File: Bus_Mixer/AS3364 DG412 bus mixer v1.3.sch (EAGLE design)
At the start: 121 parts, among them IC1 PCA9539PW, IC10 DG412-J, IC11 DG412-J, IC2 TL074JT, IC3 TL072JT, IC4 TL074JT, IC5 TL072JT, IC6 TL072JT, IC8 DG412-J, IC9 DG412-J

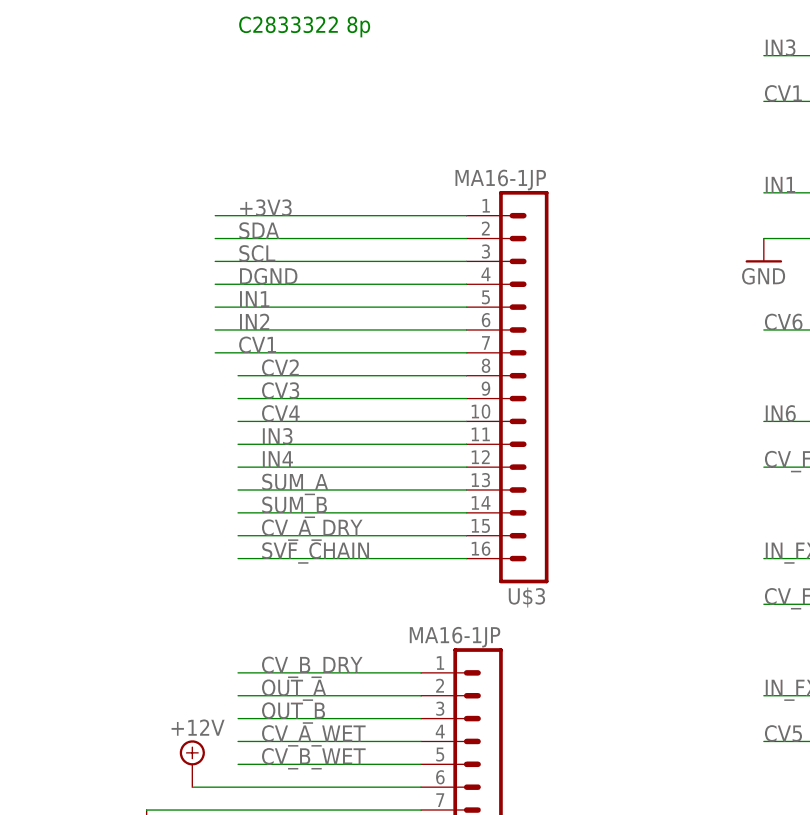
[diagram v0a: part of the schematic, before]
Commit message: Changed connector values
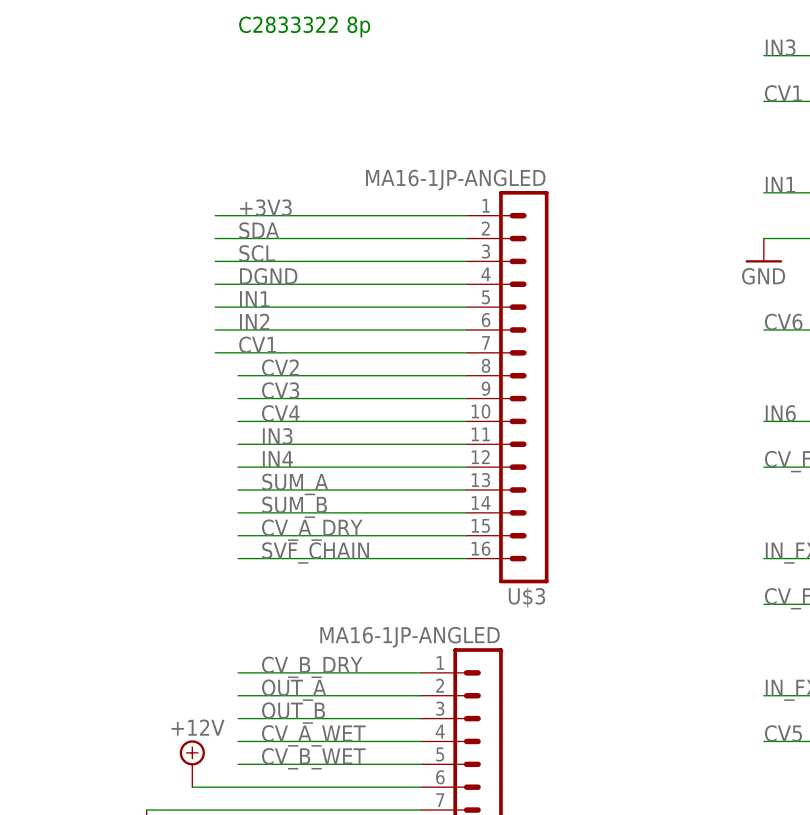
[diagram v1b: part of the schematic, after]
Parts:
- U$2, U$3: value MA16-1JP -> MA16-1JP-ANGLED
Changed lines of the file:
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@@
 <part name="IC5" library="joakim" deviceset="TL072J" device="T" value="TL072JT"/>
 <part name="R69" library="rcl" library_urn="urn:adsk.eagle:library:334" deviceset="R-EU_" device="R0402" package3d_urn="urn:adsk.eagle:package:23547/3" value="47k"/>
-<part name="U$2" library="joakim" deviceset="MA16-1J" device="P"/>
-<part name="U$3" library="joakim" deviceset="MA16-1J" device="P"/>
+<part name="U$2" library="joakim" deviceset="MA16-1J" device="P" value="MA16-1JP-ANGLED"/>
+<part name="U$3" library="joakim" deviceset="MA16-1J" device="P" value="MA16-1JP-ANGLED"/>
 </parts>
 <sheets>

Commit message: Updated
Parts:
- C13, C14, C15, C24, C25, C26, C27: device joakim:C-EU-J -> joakim:C-EU-J0402
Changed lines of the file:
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@@
 <part name="IC3" library="joakim" deviceset="TL072J" device="T" value="TL072JT"/>
 <part name="C18" library="rcl" library_urn="urn:adsk.eagle:library:334" deviceset="C-EU" device="C0402" package3d_urn="urn:adsk.eagle:package:23626/2" value="100nF"/>
-<part name="C13" library="joakim" deviceset="C-EU-J" device="" value="5nF"/>
+<part name="C13" library="joakim" deviceset="C-EU-J" device="0402" value="5nF"/>
 <part name="GND9" library="supply1" library_urn="urn:adsk.eagle:library:371" deviceset="GND" device=""/>
 <part name="DA2" library="joakim" deviceset="AS3364" device="D"/>
@@
 <part name="GND17" library="supply1" library_urn="urn:adsk.eagle:library:371" deviceset="GND" device=""/>
 <part name="GND18" library="supply1" library_urn="urn:adsk.eagle:library:371" deviceset="GND" device=""/>
-<part name="C14" library="joakim" deviceset="C-EU-J" device="" value="5nF"/>
+<part name="C14" library="joakim" deviceset="C-EU-J" device="0402" value="5nF"/>
 <part name="GND19" library="supply1" library_urn="urn:adsk.eagle:library:371" deviceset="GND" device=""/>
 <part name="DA3" library="joakim" deviceset="AS3364" device="D"/>
@@
 <part name="GND37" library="supply1" library_urn="urn:adsk.eagle:library:371" deviceset="GND" device=""/>
 <part name="IC6" library="joakim" deviceset="TL072J" device="T" value="TL072JT"/>
-<part name="C15" library="joakim" deviceset="C-EU-J" device="" value="5nF"/>
+<part name="C15" library="joakim" deviceset="C-EU-J" device="0402" value="5nF"/>
 <part name="GND38" library="supply1" library_urn="urn:adsk.eagle:library:371" deviceset="GND" device=""/>
 <part name="DA1" library="joakim" deviceset="AS3364" device="D"/>
@@
 <part name="GND13" library="supply1" library_urn="urn:adsk.eagle:library:371" deviceset="GND" device=""/>
 <part name="GND14" library="supply1" library_urn="urn:adsk.eagle:library:371" deviceset="GND" device=""/>
-<part name="C24" library="joakim" deviceset="C-EU-J" device="" value="33pF"/>
-<part name="C25" library="joakim" deviceset="C-EU-J" device="" value="33pF"/>
-<part name="C26" library="joakim" deviceset="C-EU-J" device="" value="33pF"/>
-<part name="C27" library="joakim" deviceset="C-EU-J" device="" value="33pF"/>
+<part name="C24" library="joakim" deviceset="C-EU-J" device="0402" value="33pF"/>
+<part name="C25" library="joakim" deviceset="C-EU-J" device="0402" value="33pF"/>
+<part name="C26" library="joakim" deviceset="C-EU-J" device="0402" value="33pF"/>
+<part name="C27" library="joakim" deviceset="C-EU-J" device="0402" value="33pF"/>
 <part name="GND26" library="supply1" library_urn="urn:adsk.eagle:library:371" deviceset="GND" device=""/>
 <part name="R49" library="rcl" library_urn="urn:adsk.eagle:library:334" deviceset="R-EU_" device="R0402" package3d_urn="urn:adsk.eagle:package:23547/3" value="47k"/>

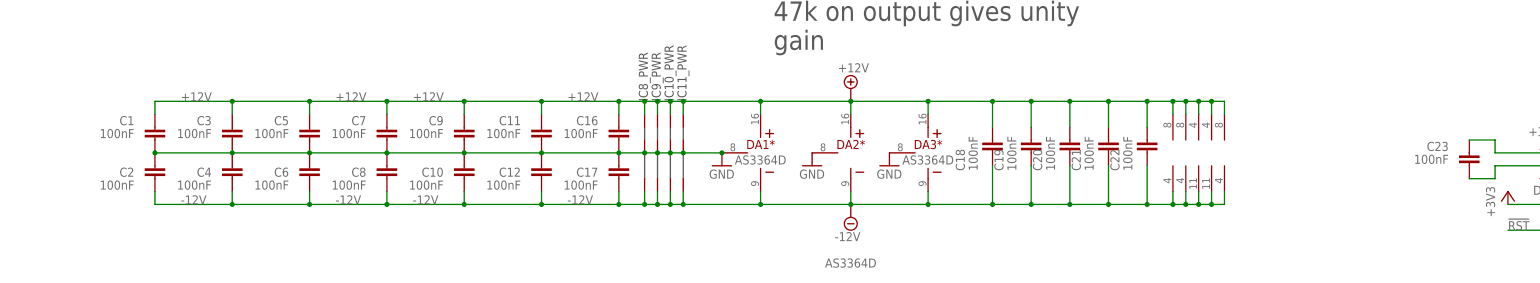
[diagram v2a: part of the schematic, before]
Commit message: Updated decoupling caps. Tested with JLCPCB
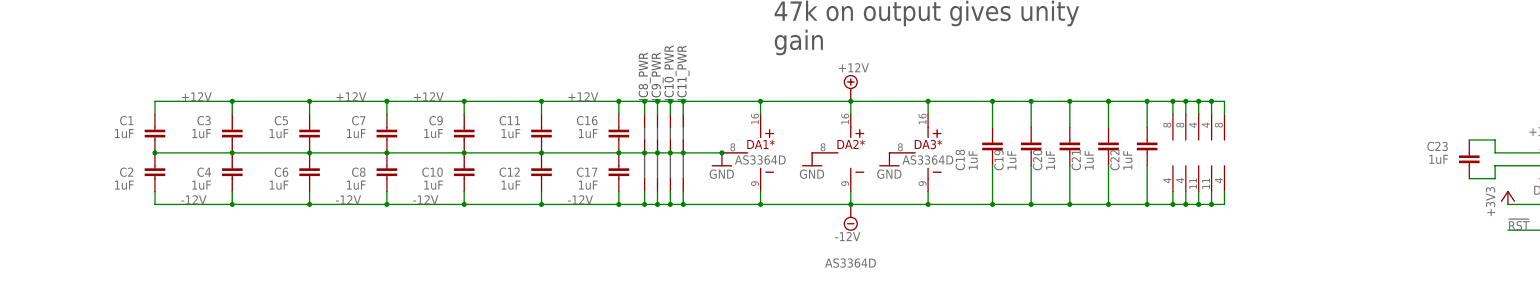
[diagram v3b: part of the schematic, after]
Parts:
- C1, C10, C11, C12, C16, C17, C2, C3, C4, C5, C6, C7, C8, C9: value 100nF -> 1uF; device rcl:C-EUC0402 -> joakim:C-EU-J0402
- C18, C19, C20, C21, C22, C23: value 100nF -> 1uF
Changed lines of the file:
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@@
 <part name="R3" library="rcl" library_urn="urn:adsk.eagle:library:334" deviceset="R-EU_" device="R0402" package3d_urn="urn:adsk.eagle:package:23547/3" value="22k"/>
 <part name="R6" library="rcl" library_urn="urn:adsk.eagle:library:334" deviceset="R-EU_" device="R0402" package3d_urn="urn:adsk.eagle:package:23547/3" value="22k"/>
-<part name="C17" library="rcl" library_urn="urn:adsk.eagle:library:334" deviceset="C-EU" device="C0402" package3d_urn="urn:adsk.eagle:package:23626/2" value="100nF"/>
-<part name="C16" library="rcl" library_urn="urn:adsk.eagle:library:334" deviceset="C-EU" device="C0402" package3d_urn="urn:adsk.eagle:package:23626/2" value="100nF"/>
+<part name="C17" library="joakim" deviceset="C-EU-J" device="0402" value="1uF"/>
+<part name="C16" library="joakim" deviceset="C-EU-J" device="0402" value="1uF"/>
 <part name="R38" library="rcl" library_urn="urn:adsk.eagle:library:334" deviceset="R-EU_" device="R0402" package3d_urn="urn:adsk.eagle:package:23547/3" value="100R"/>
 <part name="GND5" library="supply1" library_urn="urn:adsk.eagle:library:371" deviceset="GND" device=""/>
@@
 <part name="GND7" library="supply1" library_urn="urn:adsk.eagle:library:371" deviceset="GND" device=""/>
 <part name="GND8" library="supply1" library_urn="urn:adsk.eagle:library:371" deviceset="GND" device=""/>
-<part name="C19" library="rcl" library_urn="urn:adsk.eagle:library:334" deviceset="C-EU" device="C0402" package3d_urn="urn:adsk.eagle:package:23626/2" value="100nF"/>
+<part name="C19" library="rcl" library_urn="urn:adsk.eagle:library:334" deviceset="C-EU" device="C0402" package3d_urn="urn:adsk.eagle:package:23626/2" value="1uF"/>
 <part name="GND10" library="supply1" library_urn="urn:adsk.eagle:library:371" deviceset="GND" device=""/>
 <part name="IC3" library="joakim" deviceset="TL072J" device="T" value="TL072JT"/>
-<part name="C18" library="rcl" library_urn="urn:adsk.eagle:library:334" deviceset="C-EU" device="C0402" package3d_urn="urn:adsk.eagle:package:23626/2" value="100nF"/>
+<part name="C18" library="rcl" library_urn="urn:adsk.eagle:library:334" deviceset="C-EU" device="C0402" package3d_urn="urn:adsk.eagle:package:23626/2" value="1uF"/>
 <part name="C13" library="joakim" deviceset="C-EU-J" device="0402" value="5nF"/>
 <part name="GND9" library="supply1" library_urn="urn:adsk.eagle:library:371" deviceset="GND" device=""/>
@@
 <part name="R67" library="rcl" library_urn="urn:adsk.eagle:library:334" deviceset="R-EU_" device="R0402" package3d_urn="urn:adsk.eagle:package:23547/3" value="47k"/>
 <part name="R65" library="rcl" library_urn="urn:adsk.eagle:library:334" deviceset="R-EU_" device="R0402" package3d_urn="urn:adsk.eagle:package:23547/3" value="47k"/>
-<part name="C20" library="rcl" library_urn="urn:adsk.eagle:library:334" deviceset="C-EU" device="C0402" package3d_urn="urn:adsk.eagle:package:23626/2" value="100nF"/>
-<part name="C21" library="rcl" library_urn="urn:adsk.eagle:library:334" deviceset="C-EU" device="C0402" package3d_urn="urn:adsk.eagle:package:23626/2" value="100nF"/>
-<part name="C22" library="rcl" library_urn="urn:adsk.eagle:library:334" deviceset="C-EU" device="C0402" package3d_urn="urn:adsk.eagle:package:23626/2" value="100nF"/>
+<part name="C20" library="rcl" library_urn="urn:adsk.eagle:library:334" deviceset="C-EU" device="C0402" package3d_urn="urn:adsk.eagle:package:23626/2" value="1uF"/>
+<part name="C21" library="rcl" library_urn="urn:adsk.eagle:library:334" deviceset="C-EU" device="C0402" package3d_urn="urn:adsk.eagle:package:23626/2" value="1uF"/>
+<part name="C22" library="rcl" library_urn="urn:adsk.eagle:library:334" deviceset="C-EU" device="C0402" package3d_urn="urn:adsk.eagle:package:23626/2" value="1uF"/>
 <part name="GND20" library="supply1" library_urn="urn:adsk.eagle:library:371" deviceset="GND" device=""/>
-<part name="C11" library="rcl" library_urn="urn:adsk.eagle:library:334" deviceset="C-EU" device="C0402" package3d_urn="urn:adsk.eagle:package:23626/2" value="100nF"/>
-<part name="C12" library="rcl" library_urn="urn:adsk.eagle:library:334" deviceset="C-EU" device="C0402" package3d_urn="urn:adsk.eagle:package:23626/2" value="100nF"/>
+<part name="C11" library="joakim" deviceset="C-EU-J" device="0402" value="1uF"/>
+<part name="C12" library="joakim" deviceset="C-EU-J" device="0402" value="1uF"/>
 <part name="GND27" library="supply1" library_urn="urn:adsk.eagle:library:371" deviceset="GND" device=""/>
 <part name="GND28" library="supply1" library_urn="urn:adsk.eagle:library:371" deviceset="GND" device=""/>
@@
 <part name="R1" library="rcl" library_urn="urn:adsk.eagle:library:334" deviceset="R-EU_" device="R0402" package3d_urn="urn:adsk.eagle:package:23547/3" value="10k"/>
 <part name="+3V21" library="supply1" library_urn="urn:adsk.eagle:library:371" deviceset="+3V3" device=""/>
-<part name="C10" library="rcl" library_urn="urn:adsk.eagle:library:334" deviceset="C-EU" device="C0402" package3d_urn="urn:adsk.eagle:package:23626/2" value="100nF"/>
-<part name="C9" library="rcl" library_urn="urn:adsk.eagle:library:334" deviceset="C-EU" device="C0402" package3d_urn="urn:adsk.eagle:package:23626/2" value="100nF"/>
-<part name="C7" library="rcl" library_urn="urn:adsk.eagle:library:334" deviceset="C-EU" device="C0402" package3d_urn="urn:adsk.eagle:package:23626/2" value="100nF"/>
-<part name="C8" library="rcl" library_urn="urn:adsk.eagle:library:334" deviceset="C-EU" device="C0402" package3d_urn="urn:adsk.eagle:package:23626/2" value="100nF"/>
-<part name="C5" library="rcl" library_urn="urn:adsk.eagle:library:334" deviceset="C-EU" device="C0402" package3d_urn="urn:adsk.eagle:package:23626/2" value="100nF"/>
-<part name="C6" library="rcl" library_urn="urn:adsk.eagle:library:334" deviceset="C-EU" device="C0402" package3d_urn="urn:adsk.eagle:package:23626/2" value="100nF"/>
-<part name="C4" library="rcl" library_urn="urn:adsk.eagle:library:334" deviceset="C-EU" device="C0402" package3d_urn="urn:adsk.eagle:package:23626/2" value="100nF"/>
-<part name="C3" library="rcl" library_urn="urn:adsk.eagle:library:334" deviceset="C-EU" device="C0402" package3d_urn="urn:adsk.eagle:package:23626/2" value="100nF"/>
-<part name="C1" library="rcl" library_urn="urn:adsk.eagle:library:334" deviceset="C-EU" device="C0402" package3d_urn="urn:adsk.eagle:package:23626/2" value="100nF"/>
-<part name="C2" library="rcl" library_urn="urn:adsk.eagle:library:334" deviceset="C-EU" device="C0402" package3d_urn="urn:adsk.eagle:package:23626/2" value="100nF"/>
+<part name="C10" library="joakim" deviceset="C-EU-J" device="0402" value="1uF"/>
+<part name="C9" library="joakim" deviceset="C-EU-J" device="0402" value="1uF"/>
+<part name="C7" library="joakim" deviceset="C-EU-J" device="0402" value="1uF"/>
+<part name="C8" library="joakim" deviceset="C-EU-J" device="0402" value="1uF"/>
+<part name="C5" library="joakim" deviceset="C-EU-J" device="0402" value="1uF"/>
+<part name="C6" library="joakim" deviceset="C-EU-J" device="0402" value="1uF"/>
+<part name="C4" library="joakim" deviceset="C-EU-J" device="0402" value="1uF"/>
+<part name="C3" library="joakim" deviceset="C-EU-J" device="0402" value="1uF"/>
+<part name="C1" library="joakim" deviceset="C-EU-J" device="0402" value="1uF"/>
+<part name="C2" library="joakim" deviceset="C-EU-J" device="0402" value="1uF"/>
 <part name="GND21" library="supply1" library_urn="urn:adsk.eagle:library:371" deviceset="GND" device=""/>
 <part name="R77" library="rcl" library_urn="urn:adsk.eagle:library:334" deviceset="R-EU_" device="R0402" package3d_urn="urn:adsk.eagle:package:23547/3" value="47k"/>
@@
 <part name="IC2" library="joakim" deviceset="TL074J" device="T"/>
 <part name="IC4" library="joakim" deviceset="TL074J" device="T"/>
-<part name="C23" library="rcl" library_urn="urn:adsk.eagle:library:334" deviceset="C-EU" device="C0402" package3d_urn="urn:adsk.eagle:package:23626/2" value="100nF"/>
+<part name="C23" library="rcl" library_urn="urn:adsk.eagle:library:334" deviceset="C-EU" device="C0402" package3d_urn="urn:adsk.eagle:package:23626/2" value="1uF"/>
 <part name="GND40" library="supply1" library_urn="urn:adsk.eagle:library:371" deviceset="GND" device=""/>
 <part name="SUPPLY3" library="supply2" library_urn="urn:adsk.eagle:library:372" deviceset="+12V" device=""/>

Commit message: Fixed extended resistor
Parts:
- R73, R74, R75, R76: device rcl:R-EU_R0402 -> rcl:R-EU_R0603
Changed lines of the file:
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@@
 <part name="GND27" library="supply1" library_urn="urn:adsk.eagle:library:371" deviceset="GND" device=""/>
 <part name="GND28" library="supply1" library_urn="urn:adsk.eagle:library:371" deviceset="GND" device=""/>
-<part name="R73" library="rcl" library_urn="urn:adsk.eagle:library:334" deviceset="R-EU_" device="R0402" package3d_urn="urn:adsk.eagle:package:23547/3" value="220k"/>
-<part name="R74" library="rcl" library_urn="urn:adsk.eagle:library:334" deviceset="R-EU_" device="R0402" package3d_urn="urn:adsk.eagle:package:23547/3" value="220k"/>
+<part name="R73" library="rcl" library_urn="urn:adsk.eagle:library:334" deviceset="R-EU_" device="R0603" package3d_urn="urn:adsk.eagle:package:23555/3" value="220k"/>
+<part name="R74" library="rcl" library_urn="urn:adsk.eagle:library:334" deviceset="R-EU_" device="R0603" package3d_urn="urn:adsk.eagle:package:23555/3" value="220k"/>
 <part name="GND29" library="supply1" library_urn="urn:adsk.eagle:library:371" deviceset="GND" device=""/>
 <part name="GND30" library="supply1" library_urn="urn:adsk.eagle:library:371" deviceset="GND" device=""/>
@@
 <part name="GND22" library="supply1" library_urn="urn:adsk.eagle:library:371" deviceset="GND" device=""/>
 <part name="GND23" library="supply1" library_urn="urn:adsk.eagle:library:371" deviceset="GND" device=""/>
-<part name="R75" library="rcl" library_urn="urn:adsk.eagle:library:334" deviceset="R-EU_" device="R0402" package3d_urn="urn:adsk.eagle:package:23547/3" value="220k"/>
-<part name="R76" library="rcl" library_urn="urn:adsk.eagle:library:334" deviceset="R-EU_" device="R0402" package3d_urn="urn:adsk.eagle:package:23547/3" value="220k"/>
+<part name="R75" library="rcl" library_urn="urn:adsk.eagle:library:334" deviceset="R-EU_" device="R0603" package3d_urn="urn:adsk.eagle:package:23555/3" value="220k"/>
+<part name="R76" library="rcl" library_urn="urn:adsk.eagle:library:334" deviceset="R-EU_" device="R0603" package3d_urn="urn:adsk.eagle:package:23555/3" value="220k"/>
 <part name="GND24" library="supply1" library_urn="urn:adsk.eagle:library:371" deviceset="GND" device=""/>
 <part name="GND25" library="supply1" library_urn="urn:adsk.eagle:library:371" deviceset="GND" device=""/>
